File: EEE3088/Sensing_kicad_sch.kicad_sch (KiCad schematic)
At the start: 27 parts, among them U1 LTR-303ALS-01, U2 LTR-303ALS-01

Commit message: H_1
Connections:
- net SDA_Sense renamed SDA_Sense_1
- net SDA_Sense_1: no longer R20.2
- new net SDA_Sense_2: R20.2
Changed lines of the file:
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@@
     (effects (font (size 1.27 1.27)) (justify left bottom))
   )
-  (hierarchical_label "SDA_Sense" (shape input) (at 162.56 132.08 180) (fields_autoplaced)
+  (hierarchical_label "SDA_Sense_2" (shape input) (at 162.56 132.08 180) (fields_autoplaced)
     (effects (font (size 1.27 1.27)) (justify right))
   )
@@
     (effects (font (size 1.27 1.27)) (justify right))
   )
-  (hierarchical_label "SDA_Sense" (shape input) (at 160.02 53.34 180) (fields_autoplaced)
+  (hierarchical_label "SDA_Sense_1" (shape input) (at 160.02 53.34 180) (fields_autoplaced)
     (effects (font (size 1.27 1.27)) (justify right))
   )

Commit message: Schematic updates
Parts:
- added Q1: MMDT2222A, Package_TO_SOT_SMD:SOT-363_SC-70-6, symbol Transistor_BJT:MMDT2222A
- C3, C4: JLC Part Number (none) -> C28323; Manufacturer_Part_Number - -> CL21B105KBFNNNE; Price 0.0087 -> 0.0092
- R11, R12, R13, R18, R19, R20, R21: JLC Part Number C17168 -> C17477; Manufacturer_Part_Number 0402WGF0000TCE -> 0805W8F0000T5E; Price 0.0035 -> 0.0022
- R14, R15, R16, R17: Price 0.13 -> 0.1298
- TP10, TP11, TP6, TP7, TP8, TP9: JLC Part Number (none) -> DNP; Manufacturer_Part_Number 0 -> DNP
- U1, U2: Price 0.3887 -> 0.3762
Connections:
- net +3.3V: now also Q1.3 (C2), Q1.6 (C1); no longer R13.2, R16.1
- new net: Q1.1 (E1), R13.2
- new net: Q1.4 (E2), R16.1
- new net Analogue_Enable_1: Q1.5 (B2)
- new net Analogue_Enable_2: Q1.2 (B1)

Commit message: Schematic + PCB Update
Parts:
- R11, R12, R13, R18, R19, R20, R21: footprint Resistor_SMD:R_0402_1005Metric -> Resistor_SMD:R_0805_2012Metric
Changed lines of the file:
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@@
       (effects (font (size 1.27 1.27)) (justify right))
     )
-    (property "Footprint" "Resistor_SMD:R_0402_1005Metric" (at 102.108 114.3 90)
+    (property "Footprint" "Resistor_SMD:R_0805_2012Metric" (at 102.108 114.3 90)
       (effects (font (size 1.27 1.27)) hide)
     )
@@
       (effects (font (size 1.27 1.27)) hide)
     )
-    (property "Description" "0 Res 0805" (at 100.33 114.3 0)
+    (property "Description" "0 Resistor 0805" (at 100.33 114.3 0)
       (effects (font (size 1.27 1.27)) hide)
     )
@@
       (effects (font (size 1.27 1.27)))
     )
-    (property "Footprint" "Resistor_SMD:R_0402_1005Metric" (at 171.45 130.302 90)
+    (property "Footprint" "Resistor_SMD:R_0805_2012Metric" (at 171.45 130.302 90)
       (effects (font (size 1.27 1.27)) hide)
     )
@@
       (effects (font (size 1.27 1.27)) hide)
     )
-    (property "Description" "0 Res 0805" (at 171.45 132.08 0)
+    (property "Description" "0 Resistor 0805" (at 171.45 132.08 0)
       (effects (font (size 1.27 1.27)) hide)
     )
@@
       (effects (font (size 1.27 1.27)))
     )
-    (property "Footprint" "Resistor_SMD:R_0402_1005Metric" (at 171.45 138.938 90)
+    (property "Footprint" "Resistor_SMD:R_0805_2012Metric" (at 171.45 138.938 90)
       (effects (font (size 1.27 1.27)) hide)
     )
@@
       (effects (font (size 1.27 1.27)) hide)
     )
-    (property "Description" "0 Res 0805" (at 171.45 137.16 0)
+    (property "Description" "0 Resistor 0805" (at 171.45 137.16 0)
       (effects (font (size 1.27 1.27)) hide)
     )
@@
       (effects (font (size 1.27 1.27)))
     )
-    (property "Footprint" "Resistor_SMD:R_0402_1005Metric" (at 63.5 137.668 90)
+    (property "Footprint" "Resistor_SMD:R_0805_2012Metric" (at 63.5 137.668 90)
       (effects (font (size 1.27 1.27)) hide)
     )
@@
       (effects (font (size 1.27 1.27)) hide)
     )
-    (property "Description" "0 Res 0805" (at 63.5 135.89 0)
+    (property "Description" "0 Resistor 0805" (at 63.5 135.89 0)
       (effects (font (size 1.27 1.27)) hide)
     )
@@
       (effects (font (size 1.27 1.27)))
     )
-    (property "Footprint" "Resistor_SMD:R_0402_1005Metric" (at 171.45 60.198 90)
+    (property "Footprint" "Resistor_SMD:R_0805_2012Metric" (at 171.45 60.198 90)
       (effects (font (size 1.27 1.27)) hide)
     )
@@
       (effects (font (size 1.27 1.27)) hide)
     )
-    (property "Description" "0 Res 0805" (at 171.45 58.42 0)
+    (property "Description" "0 Resistor 0805" (at 171.45 58.42 0)
       (effects (font (size 1.27 1.27)) hide)
     )
@@
       (effects (font (size 1.27 1.27)))
     )
-    (property "Footprint" "Resistor_SMD:R_0402_1005Metric" (at 171.45 55.118 90)
+    (property "Footprint" "Resistor_SMD:R_0805_2012Metric" (at 171.45 55.118 90)
       (effects (font (size 1.27 1.27)) hide)
     )
@@
       (effects (font (size 1.27 1.27)) hide)
     )
-    (property "Description" "0 Res 0805" (at 171.45 53.34 0)
+    (property "Description" "0 Resistor 0805" (at 171.45 53.34 0)
       (effects (font (size 1.27 1.27)) hide)
     )
@@
       (effects (font (size 1.27 1.27)))
     )
-    (property "Footprint" "Resistor_SMD:R_0402_1005Metric" (at 62.23 46.482 90)
+    (property "Footprint" "Resistor_SMD:R_0805_2012Metric" (at 62.23 46.482 90)
       (effects (font (size 1.27 1.27)) hide)
     )
@@
       (effects (font (size 1.27 1.27)) hide)
     )
-    (property "Description" "0 Res 0805" (at 62.23 48.26 0)
-      (effects (font (size 1.27 1.27)) hide)
-    )
+    (property "Description" "0 Resistor 0805" (at 62.23 48.26 0)
+      (effects (font (size 1.27 1.27)) hide)
+    )

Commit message: PCB continued again
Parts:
- renumbered TP7 to TP10, TP10 to TP11, TP9 to TP12, TP11 to TP13, TP8 to TP14, TP6 to TP9, U1 to U3, U2 to U4

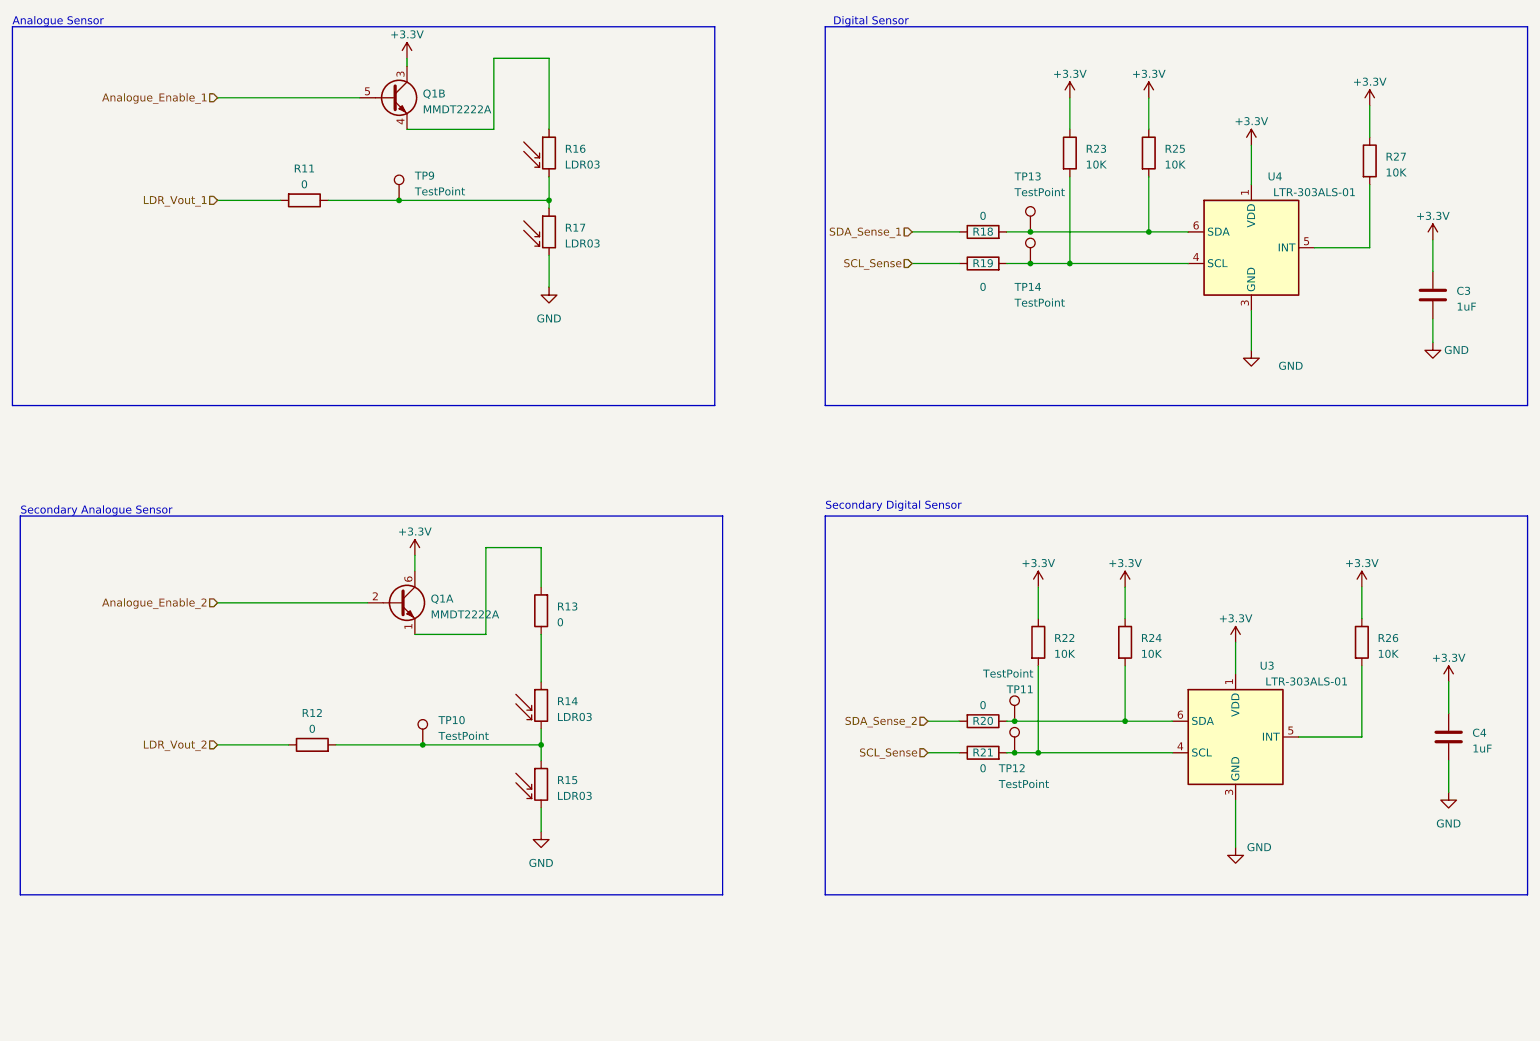
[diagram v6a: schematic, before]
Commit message: Battery footprint changed
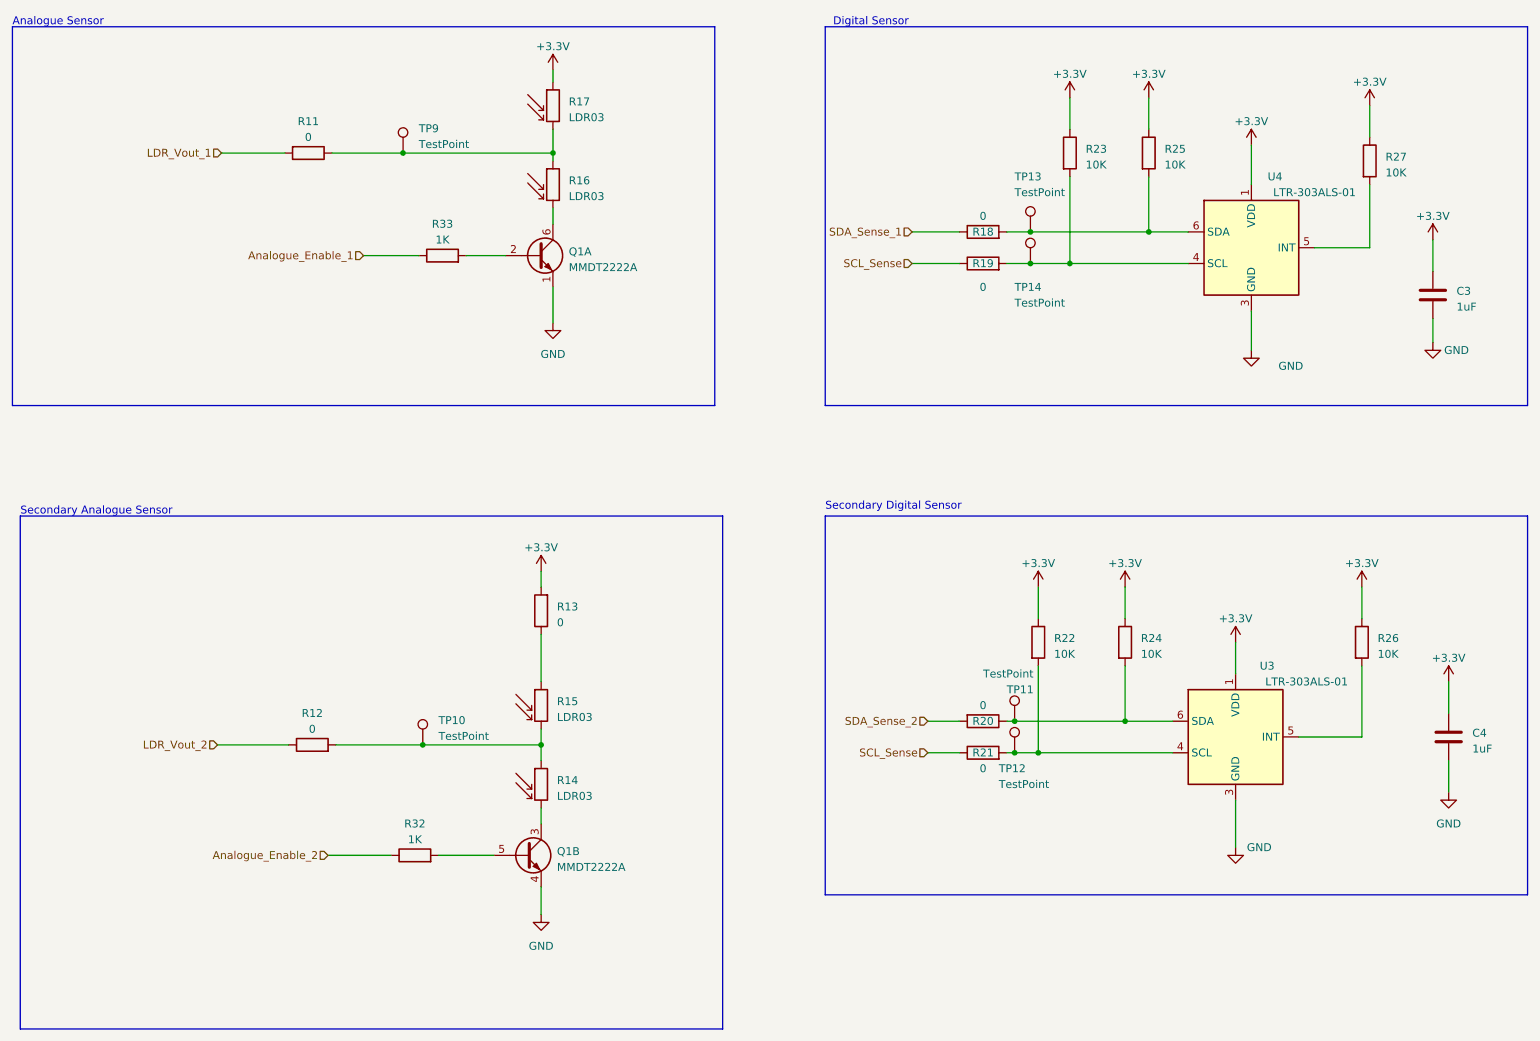
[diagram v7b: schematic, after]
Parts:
- added R32, R33: 1K, Resistor_SMD:R_0805_2012Metric, symbol Device:R
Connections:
- net +3.3V: now also R13.2, R17.1; no longer Q1.3 (C2), Q1.6 (C1)
- net Analogue_Enable_1: now also R33.1; no longer Q1.5 (B2)
- net Analogue_Enable_2: now also R32.1; no longer Q1.2 (B1)
- net GND: now also Q1.1 (E1), Q1.4 (E2); no longer R15.2, R17.2
- net at R12.2, TP10.1: now also R14.1, R15.2; no longer R14.2, R15.1
- net at R11.1, TP9.1: now also R16.1, R17.2; no longer R16.2, R17.1
- net at R13.1: now also R15.1; no longer R14.1
- new net: Q1.3 (C2), R14.2
- new net: Q1.2 (B1), R33.2
- new net: Q1.5 (B2), R32.2
- new net: Q1.6 (C1), R16.2
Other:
- moved on the sheet: Q1A, Q1B, R11, R14, R15, R16, R17, TP9
